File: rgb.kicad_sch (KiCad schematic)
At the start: 8 parts

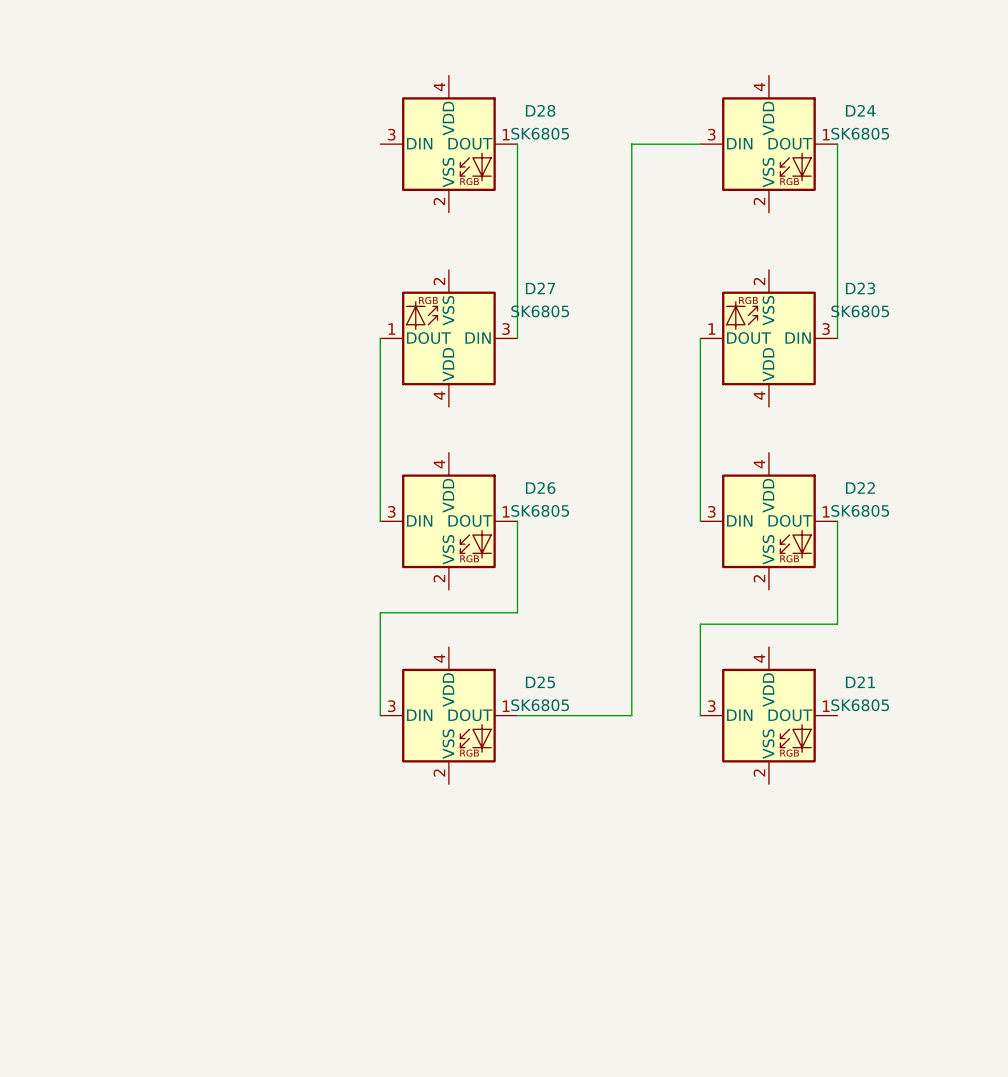
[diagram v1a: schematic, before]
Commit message: Routed RGB LED Wires
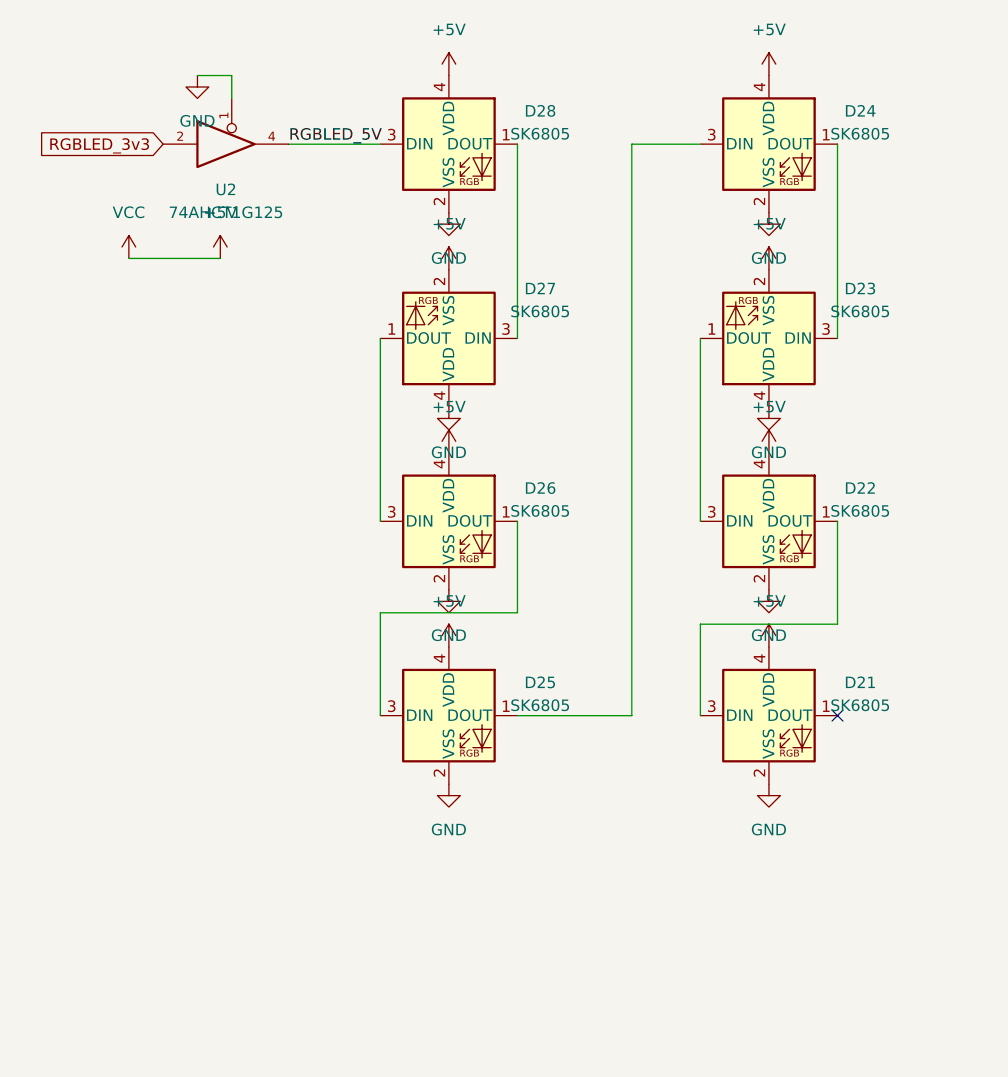
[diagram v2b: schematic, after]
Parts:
- added U2: 74AHCT1G125, Package_TO_SOT_SMD:SOT-23-5, symbol 74xGxx:74AHCT1G125
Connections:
- net GND: now reaches D21.2 (VSS)
- net GND: now also D22.2 (VSS), D23.4 (VDD), D24.2 (VSS), D25.2 (VSS), D26.2 (VSS), D27.4 (VDD), D28.2 (VSS), U2.1, U2.3 (GND)
- net +5V: now reaches D21.4 (VDD)
- net +5V: now also D22.4 (VDD), D23.2 (VSS), D24.4 (VDD), D25.4 (VDD), D26.4 (VDD), D27.2 (VSS), D28.4 (VDD), U2.5 (VCC)
- net RGBLED_5V: now reaches D28.3 (DIN)
- net RGBLED_5V: now also U2.4
- new net RGBLED_3v3: U2.2
- no-connect marks 0 -> 1

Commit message: Switched LEDS to SK6812 mini for space constraints
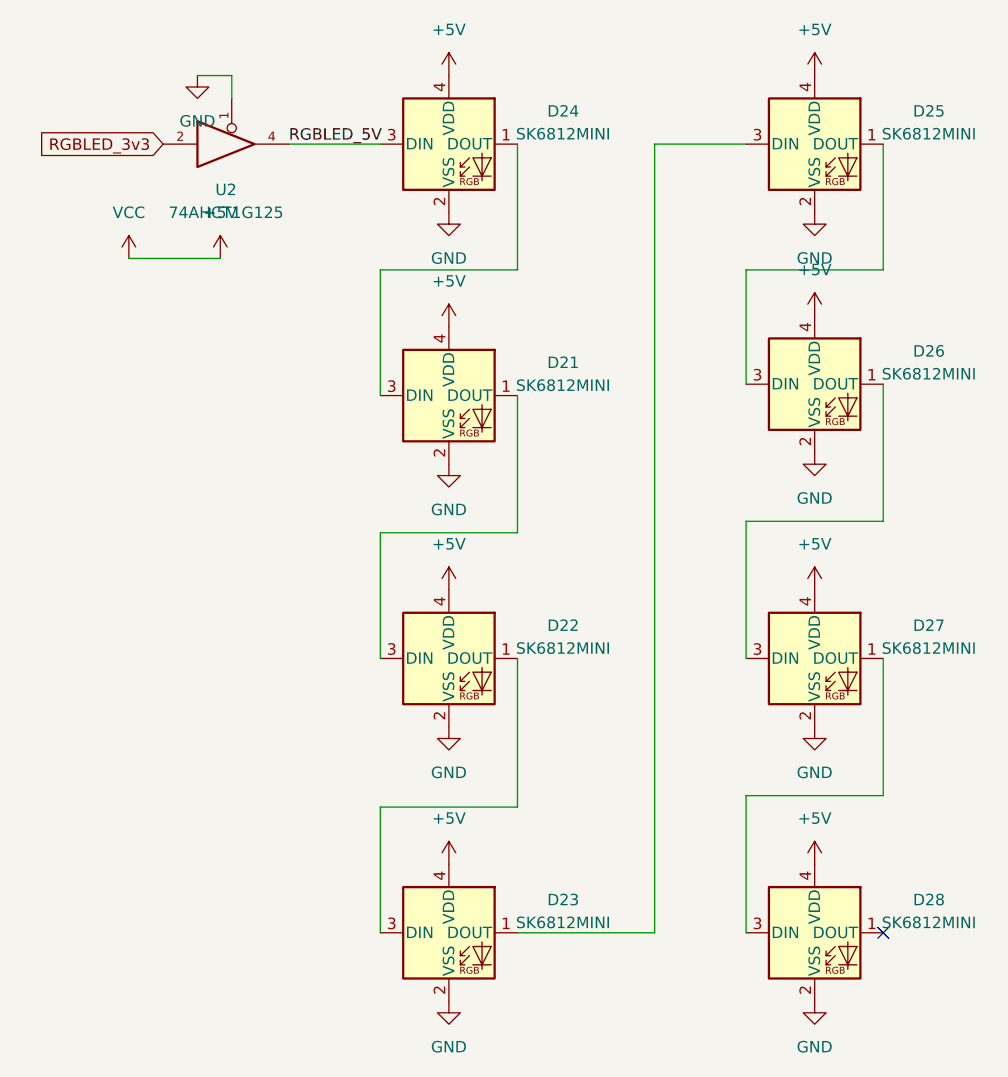
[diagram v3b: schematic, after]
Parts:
- removed D21, D22, D23, D24, D25, D26, D27, D28: SK6805, LED_SMD:LED_SK6805_PLCC4_2.4x2.7mm_P1.3mm, symbol LED:SK6805
- added D21, D22, D23, D24, D25, D26, D27, D28: SK6812MINI, LED_SMD:LED_SK6812MINI_PLCC4_3.5x3.5mm_P1.75mm, symbol LED:SK6812MINI
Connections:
- net +5V: now also D21.4 (VDD), D22.4 (VDD), D23.4 (VDD), D24.4 (VDD), D25.4 (VDD), D26.4 (VDD), D27.4 (VDD), D28.4 (VDD)
- net GND: now also D21.2 (VSS), D22.2 (VSS), D23.2 (VSS), D24.2 (VSS), D25.2 (VSS), D26.2 (VSS), D27.2 (VSS), D28.2 (VSS)
- net RGBLED_5V: now also D24.3 (DIN)
- new net: D27.1 (DOUT), D28.3 (DIN)
- new net: D26.1 (DOUT), D27.3 (DIN)
- new net: D25.1 (DOUT), D26.3 (DIN)
- new net: D23.1 (DOUT), D25.3 (DIN)
- new net: D21.3 (DIN), D24.1 (DOUT)
- new net: D22.1 (DOUT), D23.3 (DIN)
- new net: D21.1 (DOUT), D22.3 (DIN)

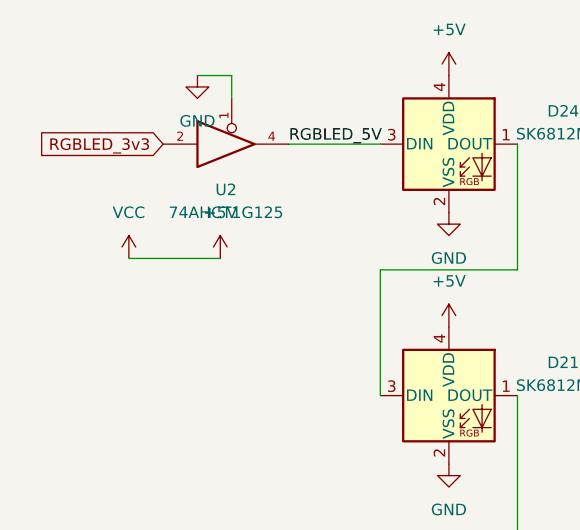
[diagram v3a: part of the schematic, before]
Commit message: updated pcb files, wired up a new usb connector in the schematic, cleaned up a couple of wiring within the schematic
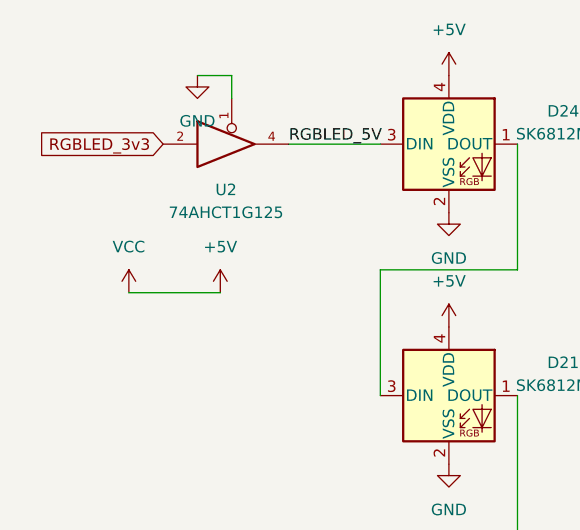
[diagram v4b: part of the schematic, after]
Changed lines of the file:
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@@
     (stroke (width 0) (type default))
   )
-  (wire (pts (xy 29.21 62.23) (xy 39.37 62.23))
+  (wire (pts (xy 29.21 66.04) (xy 39.37 66.04))
     (stroke (width 0) (type default))
   )
@@
     )
   )
-  (symbol (lib_id "power:VCC") (at 29.21 62.23 0) (mirror y) (unit 1)
-    (in_bom yes) (on_board yes) (dnp no) (fields_autoplaced)
-    (property "Reference" "#PWR019" (at 29.21 66.04 0)
-      (effects (font (size 1.27 1.27)) hide)
-    )
-    (property "Value" "VCC" (at 29.21 57.15 0)
-      (effects (font (size 1.27 1.27)))
-    )
-    (property "Footprint" "" (at 29.21 62.23 0)
-      (effects (font (size 1.27 1.27)) hide)
-    )
-    (property "Datasheet" "" (at 29.21 62.23 0)
+  (symbol (lib_id "power:VCC") (at 29.21 66.04 0) (mirror y) (unit 1)
+    (in_bom yes) (on_board yes) (dnp no) (fields_autoplaced)
+    (property "Reference" "#PWR019" (at 29.21 69.85 0)
+      (effects (font (size 1.27 1.27)) hide)
+    )
+    (property "Value" "VCC" (at 29.21 60.96 0)
+      (effects (font (size 1.27 1.27)))
+    )
+    (property "Footprint" "" (at 29.21 66.04 0)
+      (effects (font (size 1.27 1.27)) hide)
+    )
+    (property "Datasheet" "" (at 29.21 66.04 0)
       (effects (font (size 1.27 1.27)) hide)
     )
@@
     )
   )
-  (symbol (lib_id "power:+5V") (at 39.37 62.23 0) (unit 1)
-    (in_bom yes) (on_board yes) (dnp no) (fields_autoplaced)
-    (property "Reference" "#PWR021" (at 39.37 66.04 0)
-      (effects (font (size 1.27 1.27)) hide)
-    )
-    (property "Value" "+5V" (at 39.37 57.15 0)
-      (effects (font (size 1.27 1.27)))
-    )
-    (property "Footprint" "" (at 39.37 62.23 0)
-      (effects (font (size 1.27 1.27)) hide)
-    )
-    (property "Datasheet" "" (at 39.37 62.23 0)
-      (effects (font (size 1.27 1.27)) hide)
-    )
+  (symbol (lib_id "power:+5V") (at 39.37 66.04 0) (unit 1)
+    (in_bom yes) (on_board yes) (dnp no) (fields_autoplaced)
+    (property "Reference" "#PWR021" (at 39.37 69.85 0)
+      (effects (font (size 1.27 1.27)) hide)
+    )
+    (property "Value" "+5V" (at 39.37 60.96 0)
+      (effects (font (size 1.27 1.27)))
+    )
+    (property "Footprint" "" (at 39.37 66.04 0)
+      (effects (font (size 1.27 1.27)) hide)
+    )
+    (property "Datasheet" "" (at 39.37 66.04 0)
+      (effects (font (size 1.27 1.27)) hide)
+    )
